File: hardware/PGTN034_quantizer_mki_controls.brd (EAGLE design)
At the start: 69.9 x 110.5 mm, 115 parts, among them Q1 2N3904SOT23, Q2 2N3904SOT23, Q3 2N3904SOT23, Q4 2N3904SOT23, SW1 ENCODER_SW1-PEC12, SW2 ENCODER_SW1-PEC12

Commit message: set offset when changing scale
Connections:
- new net N$4: 0_RX.1, TFT1.RES
- new net N$57: 1_TX.1, U$2.P$2
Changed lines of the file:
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@@
 <wire x1="55.92" y1="91.4" x2="55.92" y2="91.56" width="0.3048" layer="16"/>
+</signal>
+<signal name="N$4">
+<contactref element="TFT1" pad="RES"/>
+<contactref element="0_RX" pad="1"/>
+<wire x1="36.195" y1="108.9025" x2="68.58" y2="88.9" width="0" layer="19" extent="1-1"/>
+</signal>
+<signal name="N$57">
+<contactref element="1_TX" pad="1"/>
+<contactref element="U$2" pad="P$2"/>
+<wire x1="35.77" y1="81.45" x2="68.58" y2="86.36" width="0" layer="19" extent="1-1"/>
 </signal>
 </signals>

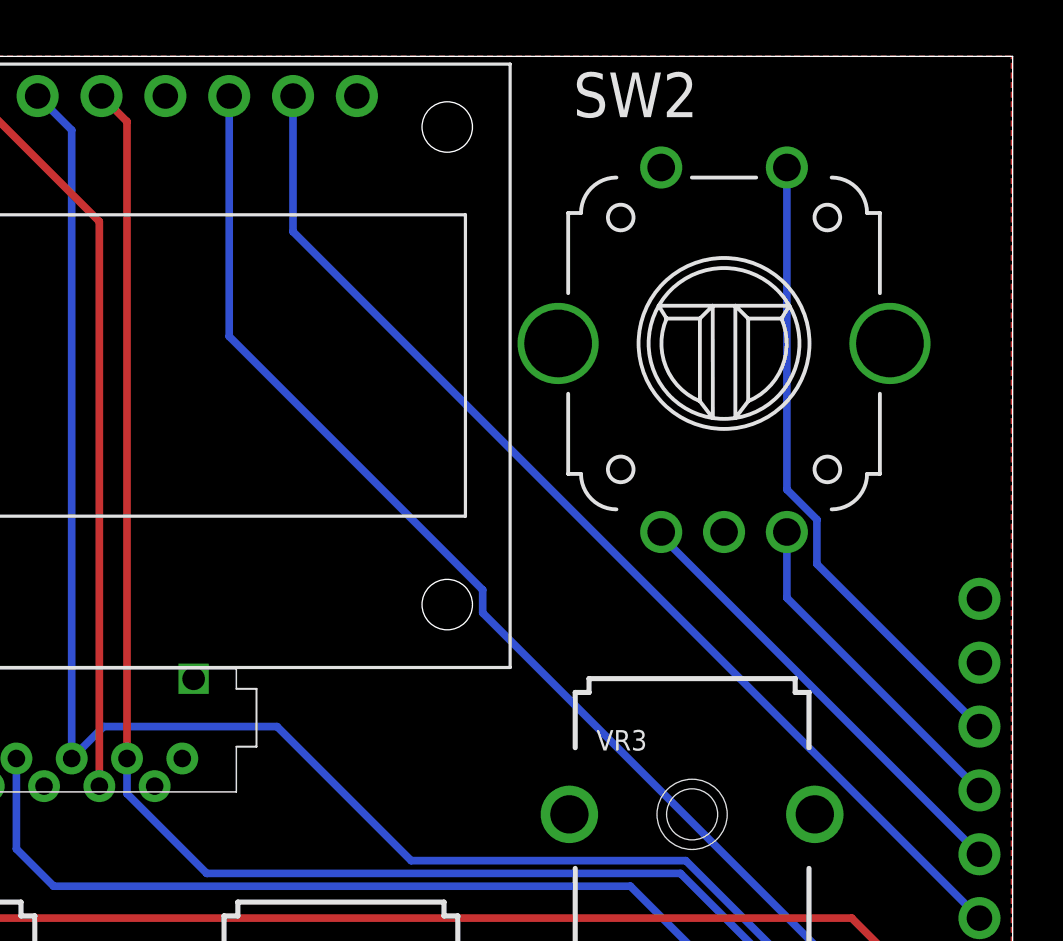
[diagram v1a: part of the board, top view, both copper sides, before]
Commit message: add sequencer controller
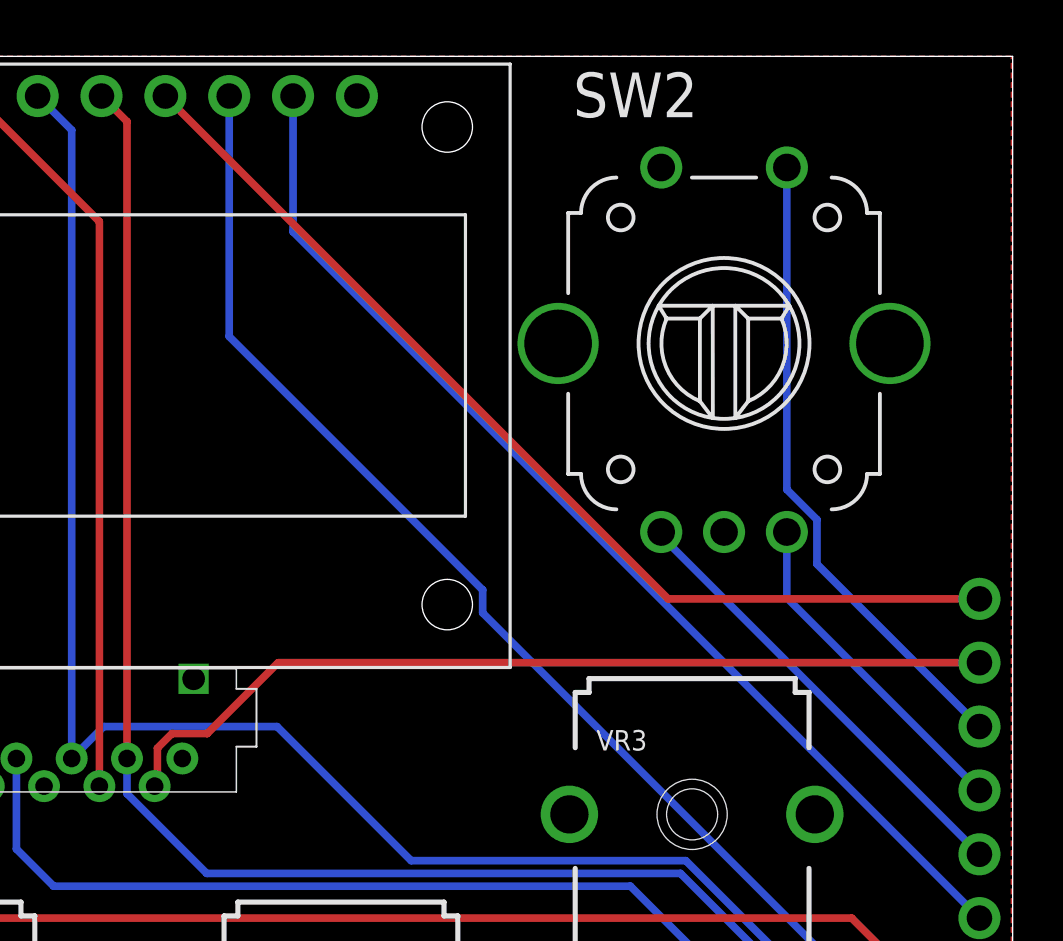
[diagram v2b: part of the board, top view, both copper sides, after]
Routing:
- net N$4: track 0.00 -> 40.7 mm
- net N$57: track 0.00 -> 35.7 mm
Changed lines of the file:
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@@
 <contactref element="TFT1" pad="RES"/>
 <contactref element="0_RX" pad="1"/>
-<wire x1="36.195" y1="108.9025" x2="68.58" y2="88.9" width="0" layer="19" extent="1-1"/>
+<wire x1="68.58" y1="88.9" x2="56.1975" y2="88.9" width="0.3048" layer="1"/>
+<wire x1="56.1975" y1="88.9" x2="36.195" y2="108.9025" width="0.3048" layer="1"/>
 </signal>
 <signal name="N$57">
 <contactref element="1_TX" pad="1"/>
 <contactref element="U$2" pad="P$2"/>
-<wire x1="35.77" y1="81.45" x2="68.58" y2="86.36" width="0" layer="19" extent="1-1"/>
+<wire x1="40.68" y1="86.36" x2="68.58" y2="86.36" width="0.3048" layer="1"/>
+<wire x1="35.8794" y1="82.960325" x2="36.459675" y2="83.5406" width="0.3048" layer="1"/>
+<wire x1="35.77" y1="81.45" x2="35.8794" y2="81.5594" width="0.3048" layer="1"/>
+<wire x1="37.8606" y1="83.5406" x2="40.68" y2="86.36" width="0.3048" layer="1"/>
+<wire x1="35.8794" y1="81.5594" x2="35.8794" y2="82.960325" width="0.3048" layer="1"/>
+<wire x1="36.459675" y1="83.5406" x2="37.8606" y2="83.5406" width="0.3048" layer="1"/>
 </signal>
 </signals>
